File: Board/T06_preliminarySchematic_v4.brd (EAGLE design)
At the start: 59.4 x 80 mm, 57 parts, among them M1 SSW-102-02-S-S, M2 SSW-102-02-S-S, Q3 2n3904, U1 ATMEGA328P_PDIP, X1 SSW-105-02-S-S, X2 SSW-102-02-S-S

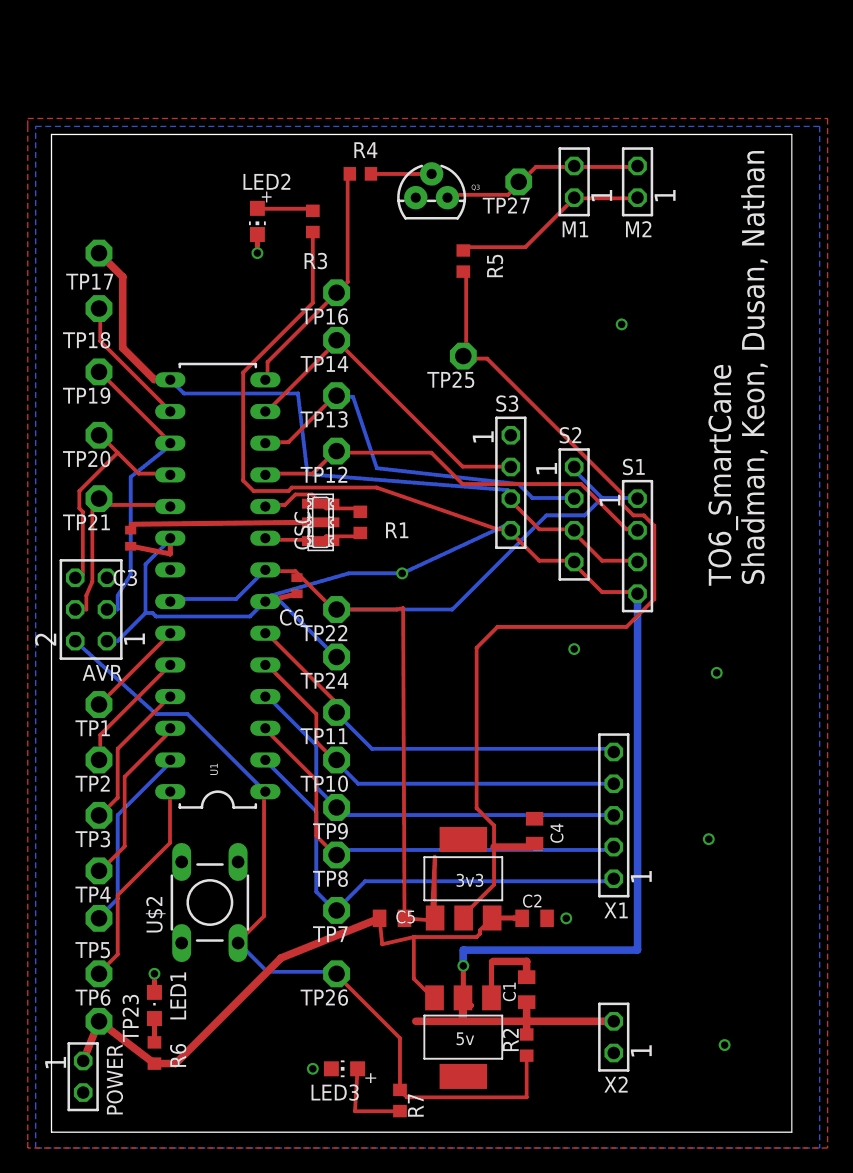
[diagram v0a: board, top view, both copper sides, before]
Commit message: Andrews suggestions implemented, still unsure what package sizes he wants us to fix
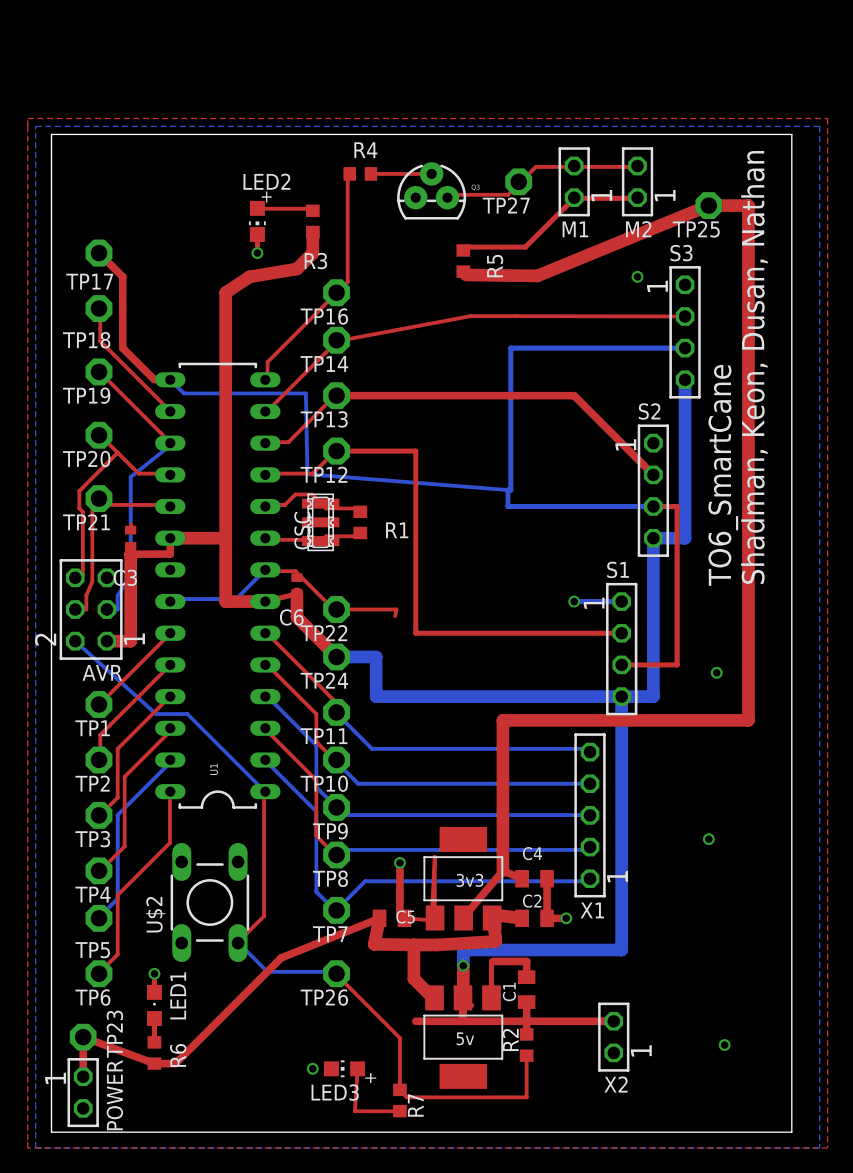
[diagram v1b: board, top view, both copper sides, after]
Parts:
- moved TP25 23.1 mm to (52.7, 74.3)
- moved S3 18.5 mm to (50.8, 64.1)
- moved S1 8.35 mm to (45.7, 38.7)
- moved S2 6.63 mm to (48.3, 51.4)
- moved C4 3.81 mm to (38.7, 20.3), turned to 0 degrees
- moved X1 1.91 mm to (43.2, 25.4)
- moved TP23 1.80 mm to (2.54, 7.62)
- moved POWER 1.27 mm to (2.54, 3.17)
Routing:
- net GND: track 117.2 -> 60.3 mm, vias 9 -> 10
- net TRIG: track 60.0 -> 104.9 mm
- net +3V3: track 76.9 -> 103.7 mm
- net ECHO1: track 33.3 -> 43.9 mm
- net ECHO3: track 26.3 -> 36.3 mm
- net ECHO2: track 31.0 -> 35.3 mm
- net BU3: track 33.3 -> 31.4 mm
- net BU1: track 35.1 -> 33.2 mm
- net BU0: track 37.8 -> 35.9 mm
- net BU4: track 32.4 -> 30.5 mm
- net +9V: track 51.0 -> 52.8 mm
- net BU2: track 33.8 -> 33.0 mm
- net +5V: track 184.9 -> 185.6 mm, vias 2 -> 1
